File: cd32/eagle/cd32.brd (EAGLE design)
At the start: 128.2 x 35.2 mm, 2 parts, among them CN1 CD32-EXPANSION, CN2 CD32-EXPANSION

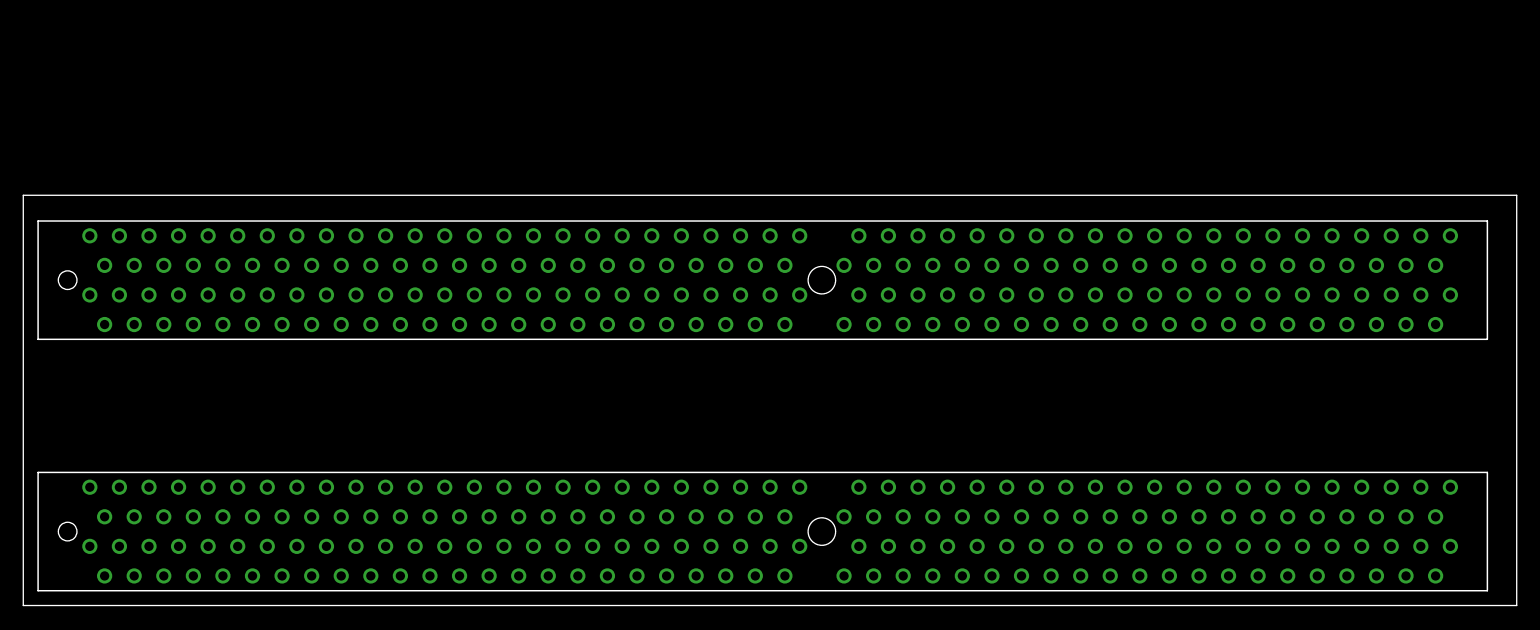
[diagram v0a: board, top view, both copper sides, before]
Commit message: fixed the stupid Dimension outline of the CD32 connector. Bare bones routed the cd32.
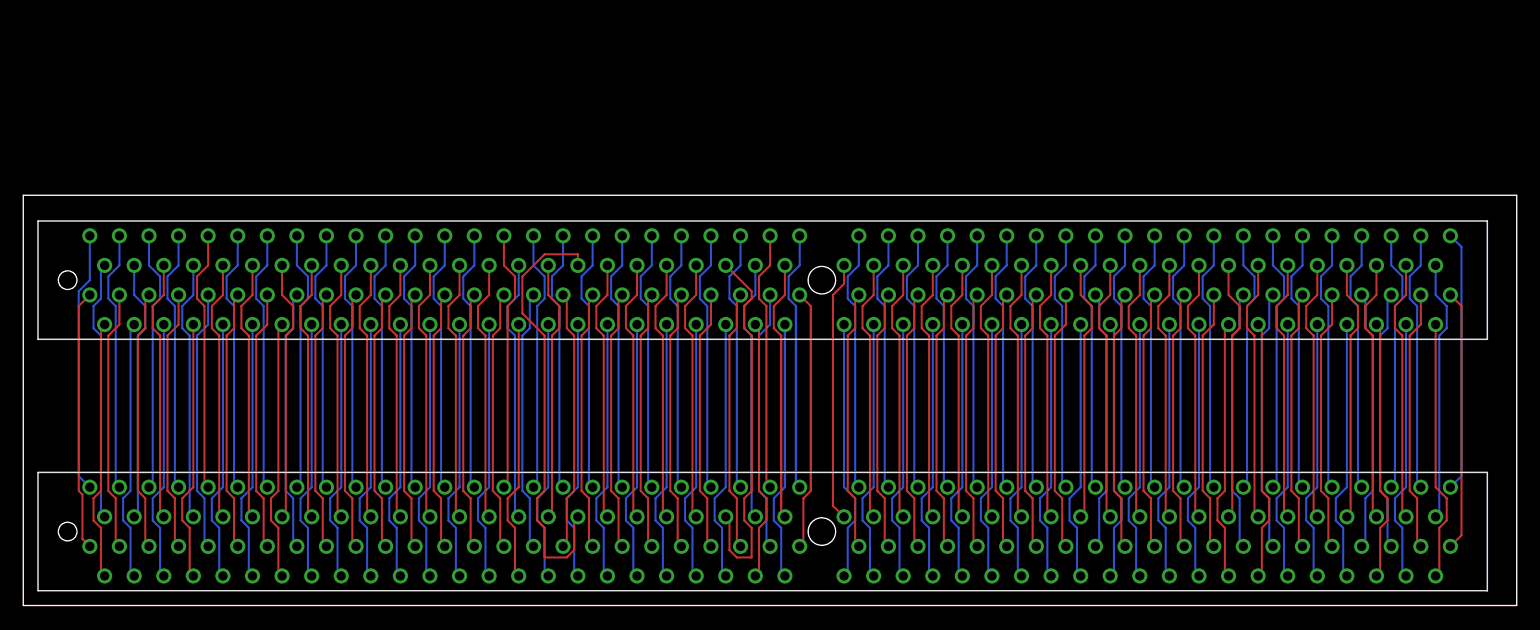
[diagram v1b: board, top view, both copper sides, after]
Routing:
- net NC@11: track 0.00 -> 37.7 mm
- net _AVEC: track 0.00 -> 32.2 mm
- net NC@3: track 0.00 -> 22.4 mm
- net NC@2: track 0.00 -> 22.4 mm
- net _TXD: track 0.00 -> 22.4 mm
- net _RST: track 0.00 -> 22.4 mm
- net _PUNT: track 0.00 -> 22.4 mm
- net _INT6: track 0.00 -> 22.4 mm
- net _FIRE1: track 0.00 -> 22.4 mm
- net _EXT_VIDEO: track 0.00 -> 22.4 mm
- net _EXP_BG: track 0.00 -> 22.4 mm
- net _DSACK_1: track 0.00 -> 22.4 mm
- net _DS: track 0.00 -> 22.4 mm
- net _DKRD: track 0.00 -> 22.4 mm
- net _CPU_BG: track 0.00 -> 22.4 mm
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
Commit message: updates.. adjusted board shape... not finished yet Added Maxim RS232 chip
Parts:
- added C1, C2, C3: (no value), eagle-ltspice:C1206
- added IC1: MAX3311, maxim:UMAX10
- moved CN1 0.58 mm to (63.5, 5.77)
- moved CN2 0.41 mm to (63.5, 28.3)
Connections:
- new net GND: C3.2, IC1.10
- new net N$1: C1.1, IC1.9
- new net N$2: C1.2, IC1.2
- new net N$3: C2.1, IC1.8
- new net VCC: C3.1, IC1.1
- net +12V@1: now also C2.2
- net _RXD: now also IC1.5
- net _TXD: now also IC1.4
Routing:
- net GND@2: track 22.4 -> 63.7 mm
- net +12V@1: track 22.4 -> 54.6 mm
- net AR: track 22.4 -> 46.9 mm
- net D6: track 22.4 -> 44.6 mm
- net _RXD: track 22.4 -> 38.0 mm
- net NC@11: track 37.7 -> 23.5 mm
- net _TXD: track 22.4 -> 35.6 mm
- net D31: track 22.4 -> 34.0 mm
- net _INT6: track 22.4 -> 34.0 mm
- net D8: track 22.4 -> 32.0 mm
- net _AVEC: track 32.2 -> 23.4 mm
- net N$1: track 0.00 -> 4.44 mm
- net N$2: track 0.00 -> 4.35 mm
- net N$3: track 0.00 -> 2.69 mm
- net GND: track 0.00 -> 2.33 mm
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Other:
- board size 128.2 x 35.2 mm -> 127.2 x 50.1 mm
- board text added: "Terrible Fire CD32 Adaptor (C) 2017 S.J Leary Publushed Under the GNU GPLv2"
